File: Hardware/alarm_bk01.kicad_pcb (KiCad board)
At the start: 2 copper layers, 65 x 22 mm, 18 parts, among them Q1 2N3904, SW1 START, SW2 Sensor, SW3 SW_SPDT, U1 ATtiny85V-10P

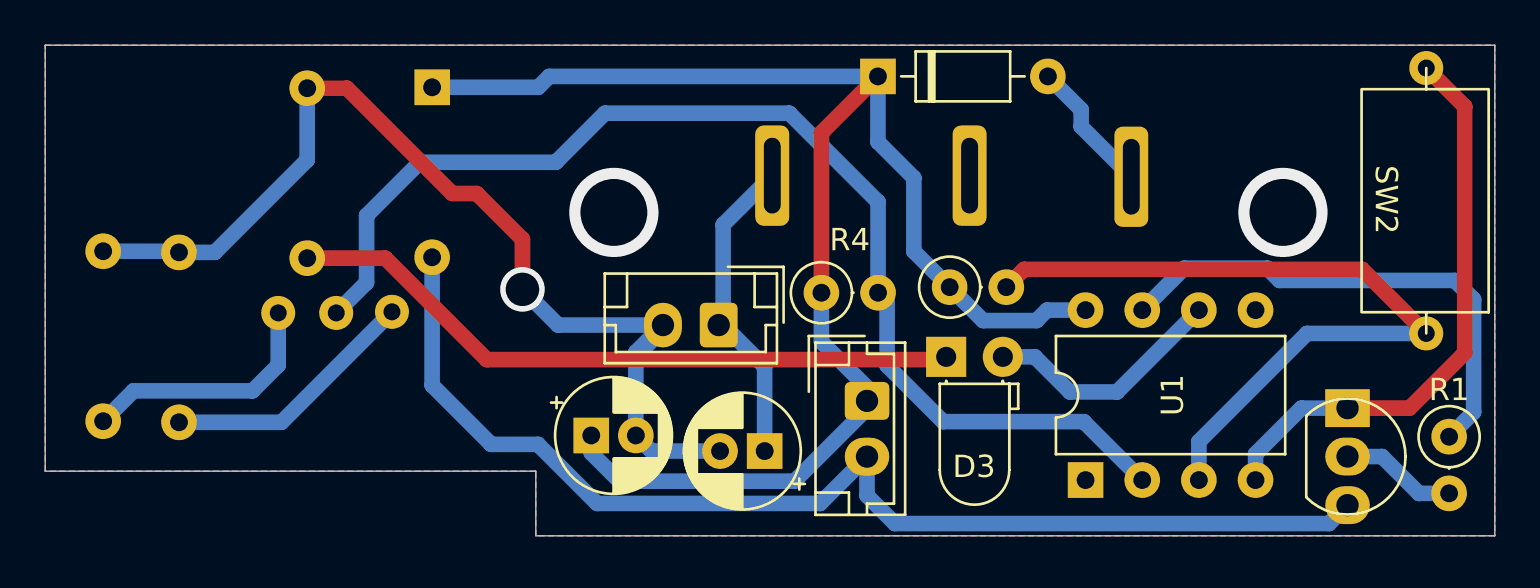
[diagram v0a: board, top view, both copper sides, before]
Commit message: reorganice components
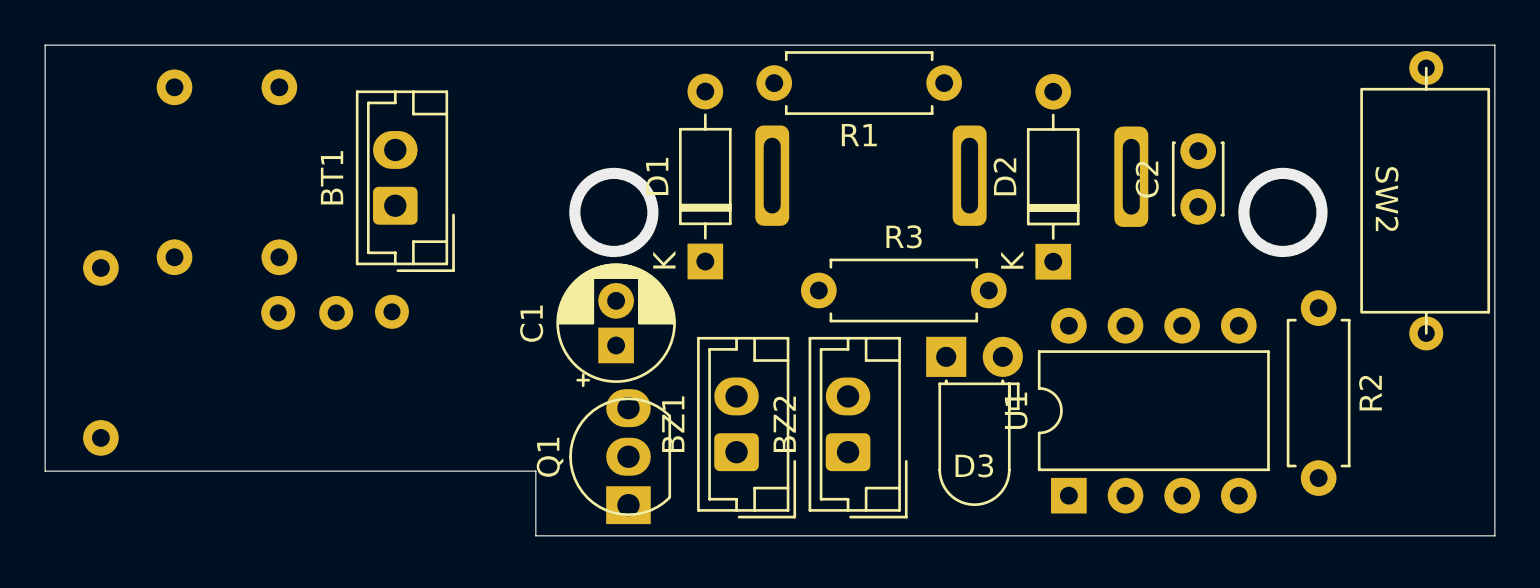
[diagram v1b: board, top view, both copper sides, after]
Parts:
- added BZ2: Buzzer, Connector_JST:JST_EH_B2B-EH-A_1x02_P2.50mm_Vertical, F.Cu at (93.8, 49.5)
- C2: value 47u -> 47uF; footprint Capacitor_THT:CP_Radial_D5.0mm_P2.00mm -> Capacitor_THT:C_Disc_D3.0mm_W2.0mm_P2.50mm
- D1, R3: moved to F.Cu
- R1, R2: footprint Resistor_THT:R_Axial_DIN0207_L6.3mm_D2.5mm_P2.54mm_Vertical -> Resistor_THT:R_Axial_DIN0207_L6.3mm_D2.5mm_P7.62mm_Horizontal
- R4: footprint Resistor_THT:R_Axial_DIN0207_L6.3mm_D2.5mm_P2.54mm_Vertical -> Resistor_THT:R_Axial_DIN0207_L6.3mm_D2.5mm_P7.62mm_Horizontal; moved to B.Cu
- moved Q1 32.3 mm to (84.0, 51.0), turned to 90 degrees
- moved R4 32.3 mm to (60.3, 41.3), turned to -90 degrees
- moved C2 29.1 mm to (109.5, 38.5), turned to 90 degrees
- moved R1 27.6 mm to (98.1, 33.0), turned to 180 degrees
- moved R3 23.0 mm to (92.5, 42.3), turned to 0 degrees
- moved R2 16.6 mm to (114.9, 43.1), turned to -90 degrees
- moved BT1 15.5 mm to (73.5, 38.5), turned to 90 degrees
- moved D1 14.5 mm to (87.4, 41.0), turned to 90 degrees
- moved D2 11.4 mm to (103.0, 41.0), turned to 90 degrees
- moved R7 10.8 mm to (68.3, 40.8)
- moved C1 8.17 mm to (83.4, 44.8), turned to 90 degrees
- moved R6 7.40 mm to (63.6, 40.8)
- moved BZ1 6.29 mm to (88.8, 49.5), turned to 90 degrees
- moved U1 1.03 mm to (103.7, 51.5)
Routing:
- net 0: track 73.6 -> 0.00 mm, vias 1 -> 0
- net VCC: track 69.7 -> 0.00 mm
- net sensibilidad: track 52.8 -> 0.00 mm
- net Net-(D1-Pad2): track 52.5 -> 0.00 mm
- net sensor: track 34.3 -> 0.00 mm
- net Net-(D3-Pad1): track 30.6 -> 0.00 mm
- net alarma: track 22.8 -> 0.00 mm
- net /POWER: track 14.0 -> 0.00 mm
- net Net-(R6-Pad1): track 11.6 -> 0.00 mm
- net Net-(R7-Pad1): track 11.2 -> 0.00 mm
- net Indicator: track 11.0 -> 0.00 mm
- net /ON_NET: track 6.05 -> 0.00 mm
- net Net-(Q1-Pad2): track 5.24 -> 0.00 mm
- removed copper zone on B.Cu, net 0
- removed copper zone on F.Cu, net 0

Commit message: finish design
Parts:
- removed BZ2: Buzzer, Connector_JST:JST_EH_B2B-EH-A_1x02_P2.50mm_Vertical
- R1, R2, R3: footprint Resistor_THT:R_Axial_DIN0207_L6.3mm_D2.5mm_P7.62mm_Horizontal -> Resistor_THT:R_Axial_DIN0204_L3.6mm_D1.6mm_P2.54mm_Vertical
- R4: footprint Resistor_THT:R_Axial_DIN0207_L6.3mm_D2.5mm_P7.62mm_Horizontal -> Resistor_THT:R_Axial_DIN0204_L3.6mm_D1.6mm_P2.54mm_Vertical; moved to F.Cu
- moved D1 34.3 mm to (120.4, 50.5), turned to 180 degrees
- moved Q1 25.6 mm to (109.5, 49.0), turned to 180 degrees
- moved R4 24.8 mm to (84.0, 48.6)
- moved BZ1 19.7 mm to (107.7, 44.0), turned to 180 degrees
- moved U1 16.1 mm to (87.6, 51.2)
- moved R1 15.9 mm to (103.5, 48.0), turned to -90 degrees
- moved D2 8.62 mm to (100.1, 32.9), turned to 0 degrees
- moved R3 8.21 mm to (100.7, 42.3), turned to 180 degrees
- moved C1 1.94 mm to (83.2, 42.8), turned to -90 degrees
- moved R2 1.39 mm to (114.9, 44.5)
- moved C2 0.85 mm to (109.2, 37.8)
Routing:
- net 0: track 0.00 -> 173.9 mm
- net VCC: track 0.00 -> 90.0 mm
- net sensor: track 0.00 -> 39.6 mm
- net /POWER: track 0.00 -> 30.8 mm
- net sensibilidad: track 0.00 -> 25.1 mm
- net alarma: track 0.00 -> 16.8 mm
- net Net-(BZ1-Pad2): track 0.00 -> 16.5 mm
- net Net-(R6-Pad1): track 0.00 -> 12.4 mm
- net Indicator: track 0.00 -> 10.8 mm
- net Net-(Q1-Pad2): track 0.00 -> 6.53 mm
- net /ON_NET: track 0.00 -> 4.80 mm
- net Net-(D3-Pad1): track 0.00 -> 4.01 mm
- net Net-(R7-Pad1): track 0.00 -> 2.52 mm
- added copper zone on B.Cu, net 0
- added copper zone on F.Cu, net 0

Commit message: update pcb model
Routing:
- net 0: track 173.9 -> 173.0 mm
- net VCC: track 90.0 -> 90.9 mm
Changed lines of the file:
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@@
       (svguseinch false)
       (svgprecision 6)
-      (excludeedgelayer false)
+      (excludeedgelayer true)
       (plotframeref false)
       (viasonmask false)
@@
       (sketchpadsonfab true)
       (subtractmaskfromsilk false)
-      (outputformat 4)
+      (outputformat 1)
       (mirror false)
       (drillshape 0)
@@
     (property "Sheetname" "")
     (attr through_hole)
-    (fp_text reference "C1" (at 1 -3.75 90) (layer "F.SilkS")
+    (fp_text reference "C1" (at 0.865336 3.7 90) (layer "F.SilkS")
       (effects (font (size 1 1) (thickness 0.15)))
     )
@@
     (fp_line (start 5 -1.6) (end -2.5 -1.6) (layer "F.Fab") (width 0.1))
     (fp_line (start -2.91 2.61) (end -0.41 2.61) (layer "F.Fab") (width 0.1))
-    (pad "1" thru_hole roundrect (at 0 0 180) (size 1.7 2) (drill 1) (layers *.Cu *.Mask) (roundrect_rratio 0.147059)
+    (pad "1" thru_hole roundrect (at 0 0 180) (size 1.7 2) (drill 1) (layers *.Cu *.Mask) (roundrect_rratio 0.1470588235)
       (net 3 "VCC") (pinfunction "-") (pintype "passive"))
     (pad "2" thru_hole oval (at 2.5 0 180) (size 1.7 2) (drill 1) (layers *.Cu *.Mask)
@@
     (fp_line (start -2.5 2.2) (end 5 2.2) (layer "F.Fab") (width 0.1))
     (fp_line (start -2.91 2.61) (end -0.41 2.61) (layer "F.Fab") (width 0.1))
-    (pad "1" thru_hole roundrect (at 0 0 90) (size 1.7 2) (drill 1) (layers *.Cu *.Mask) (roundrect_rratio 0.147059)
+    (pad "1" thru_hole roundrect (at 0 0 90) (size 1.7 2) (drill 1) (layers *.Cu *.Mask) (roundrect_rratio 0.1470588235)
       (net 1 "/POWER") (pinfunction "+") (pintype "passive"))
     (pad "2" thru_hole oval (at 2.5 0 90) (size 1.7 2) (drill 1) (layers *.Cu *.Mask)
@@
   (segment (start 75.9 41.7) (end 75.9 41.6) (width 0.7) (layer "B.Cu") (net 2))
   (segment (start 95.32 51.4) (end 93.97 52.75) (width 0.7) (layer "B.Cu") (net 2))
-  (segment (start 72.6 36) (end 73.5 36) (width 0.7) (layer "B.Cu") (net 2))
   (segment (start 63.580811 48.5) (end 59.05 43.969189) (width 0.7) (layer "B.Cu") (net 2))
   (segment (start 63.6 33.19) (end 68.3 33.19) (width 0.7) (layer "B.Cu") (net 2))
@@
   (segment (start 112.06863 42.1) (end 114.1 42.1) (width 0.7) (layer "B.Cu") (net 3))
   (segment (start 120.4 47.7) (end 120.4 50.5) (width 0.7) (layer "B.Cu") (net 3))
-  (segment (start 84 48.58) (end 84 47.18) (width 0.7) (layer "B.Cu") (net 3))
   (segment (start 114.1 42.1) (end 114.9 42.9) (width 0.7) (layer "B.Cu") (net 3))
   (segment (start 109.2 37.75) (end 109.2 39.23137) (width 0.7) (layer "B.Cu") (net 3))
@@
   (segment (start 110.88 44.48) (end 114.9 44.48) (width 0.7) (layer "B.Cu") (net 3))
   (segment (start 107.7 44) (end 110.4 44) (width 0.7) (layer "B.Cu") (net 3))
-  (segment (start 84 47.18) (end 87.6 43.58) (width 0.7) (layer "B.Cu") (net 3))
   (segment (start 114.9 42.9) (end 114.9 44.48) (width 0.7) (layer "B.Cu") (net 3))
   (segment (start 110.4 44) (end 110.88 44.48) (width 0.7) (layer "B.Cu") (net 3))
   (segment (start 100.09 32.9) (end 102 32.9) (width 0.7) (layer "B.Cu") (net 3))
   (segment (start 121.7 42.9) (end 121.7 46.4) (width 0.7) (layer "B.Cu") (net 3))
+  (segment (start 84 48.58) (end 85.28 47.3) (width 0.7) (layer "B.Cu") (net 3))
   (segment (start 117 40.8) (end 119.6 40.8) (width 0.7) (layer "B.Cu") (net 3))
+  (segment (start 87.6 46.5) (end 87.6 43.58) (width 0.7) (layer "B.Cu") (net 3))
   (segment (start 87.6 44) (end 87.6 43.58) (width 0.7) (layer "B.Cu") (net 3))
+  (segment (start 85.28 47.3) (end 86.8 47.3) (width 0.7) (layer "B.Cu") (net 3))
+  (segment (start 86.8 47.3) (end 87.6 46.5) (width 0.7) (layer "B.Cu") (net 3))
   (segment (start 109.2 39.23137) (end 109.96863 40) (width 0.7) (layer "B.Cu") (net 3))
   (segment (start 121.7 46.4) (end 120.4 47.7) (width 0.7) (layer "B.Cu") (net 3))
@@
   (segment (start 111.4 46.2) (end 107.4 46.2) (width 0.7) (layer "B.Cu") (net 4))
   (segment (start 112.78 47.58) (end 111.4 46.2) (width 0.7) (layer "B.Cu") (net 4))
-  (segment (start 105.2 45.5) (end 105.2 44) (width 0.7) (layer "B.Cu") (net 4))
   (segment (start 107.4 46.2) (end 105.9 46.2) (width 0.7) (layer "B.Cu") (net 4))
+  (segment (start 105.2 45.5) (end 105.2 44) (width 0.7) (layer "B.Cu") (net 4))
   (segment (start 105.4 44.2) (end 105.2 44) (width 0.7) (layer "B.Cu") (net 4))
   (segment (start 105.4 48.5) (end 105.4 46.7) (width 0.7) (layer "B.Cu") (net 4))
